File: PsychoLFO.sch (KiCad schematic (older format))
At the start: 17 parts

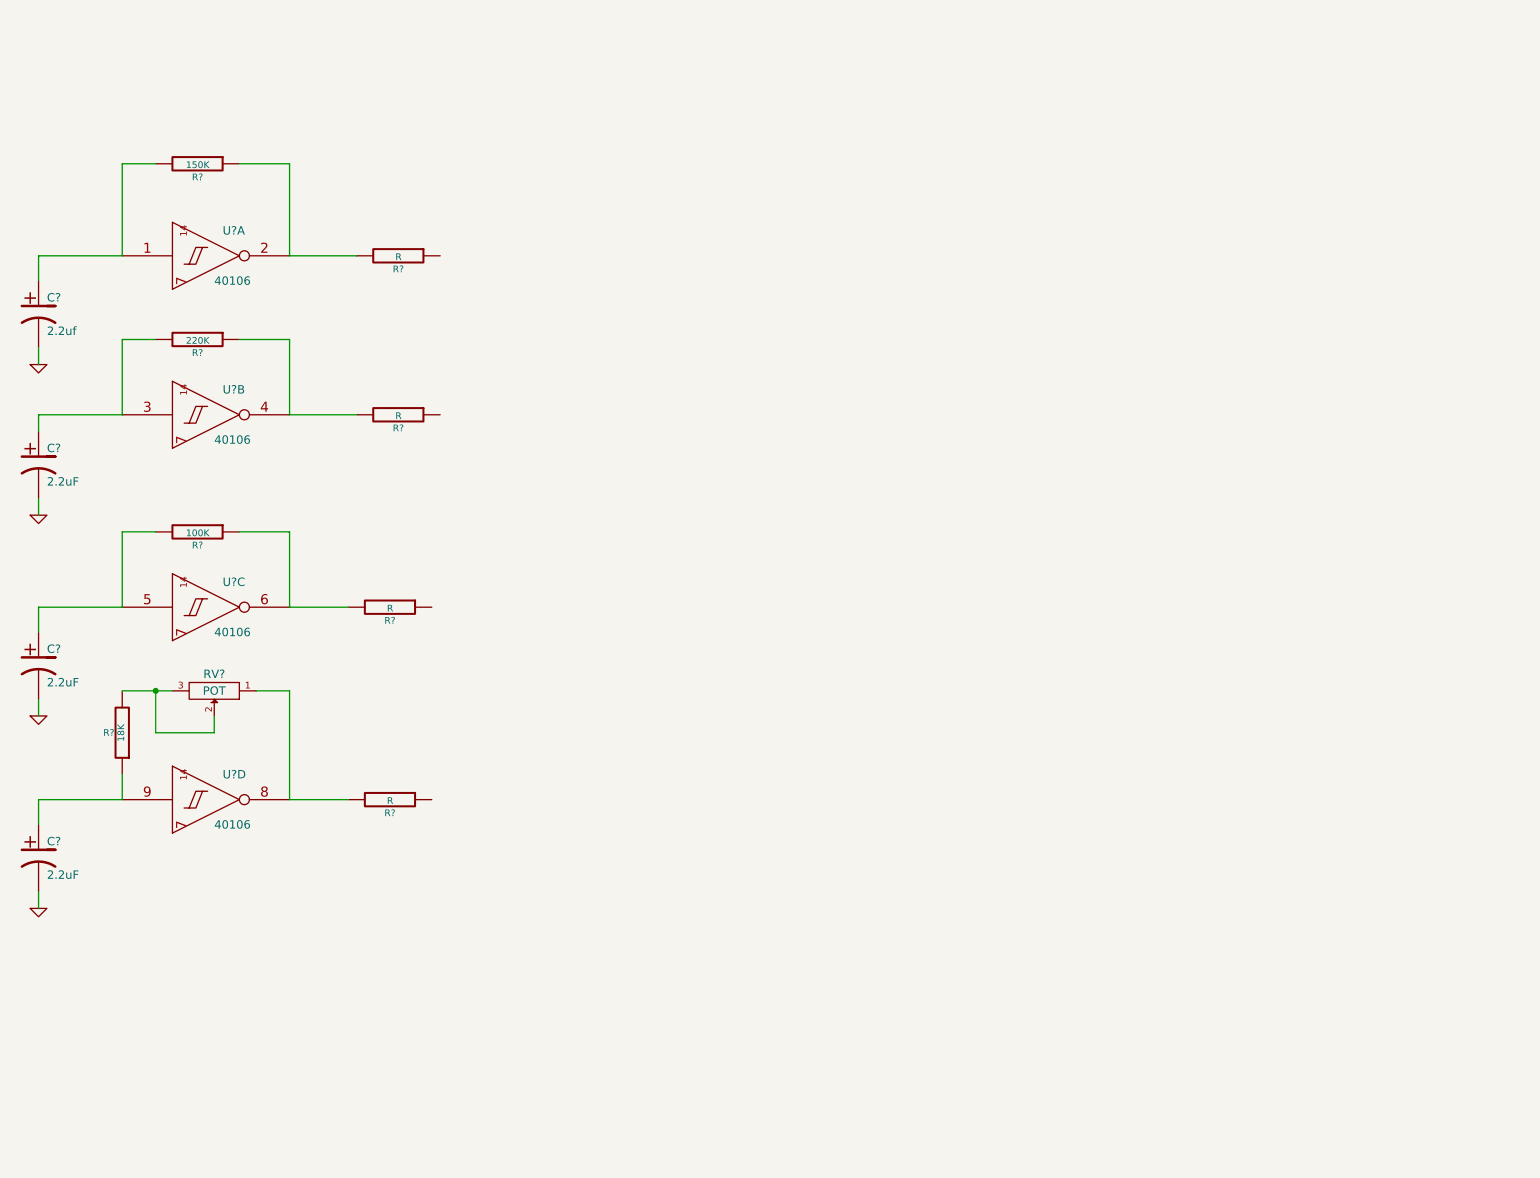
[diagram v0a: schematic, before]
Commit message: Some further progress on LFO
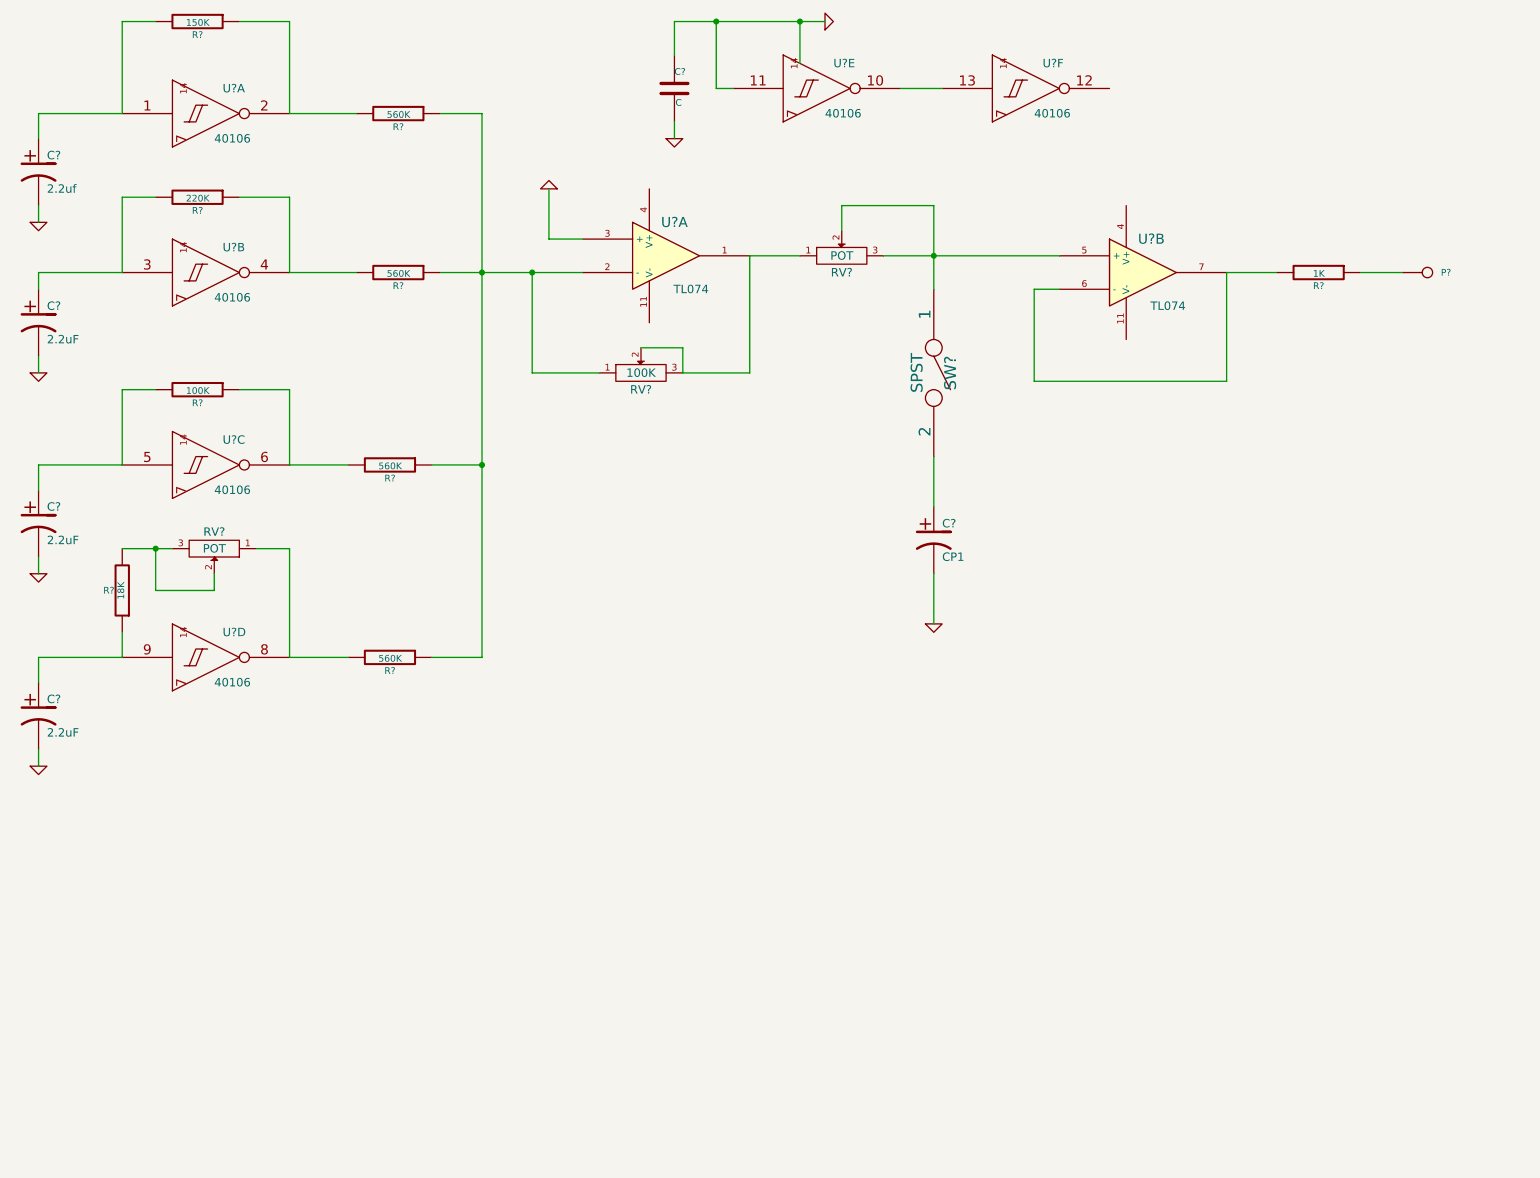
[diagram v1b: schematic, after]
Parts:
- added C?: CP1, symbol CP1
- added C?: C, symbol C
- added P?: CONN_1, symbol CONN_1
- added R?: 1K, symbol R
- added RV?: 100K, symbol POT
- added RV?: POT, symbol POT
- added SW?: SPST, symbol SPST
- added U? (x2): TL074, symbol TL074
- added U? (x2): 40106, symbol 40106
- R? (x4): value R -> 560K
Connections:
- net GND: now also C?.1, C?.2, C?.2, U?.11 (In), U?.14 (VDD), U?.3 (+)
- net at R?.1: now also R?.1, R?.1, R?.1, RV?.1, U?.2 (-)
- new net: RV?.1, RV?.2, RV?.3, U?.1
- new net: RV?.2, RV?.3, SW?.1, U?.5 (+)
- new net: C?.1, SW?.2
- new net: R?.2, U?.6 (-), U?.7
- new net: P?.1, R?.1
- new net: U?.10 (Out), U?.13 (In)
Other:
- moved on the sheet: C?, R?, RV?, U?A, U?B, U?C, U?D

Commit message: Added CV Mixer section
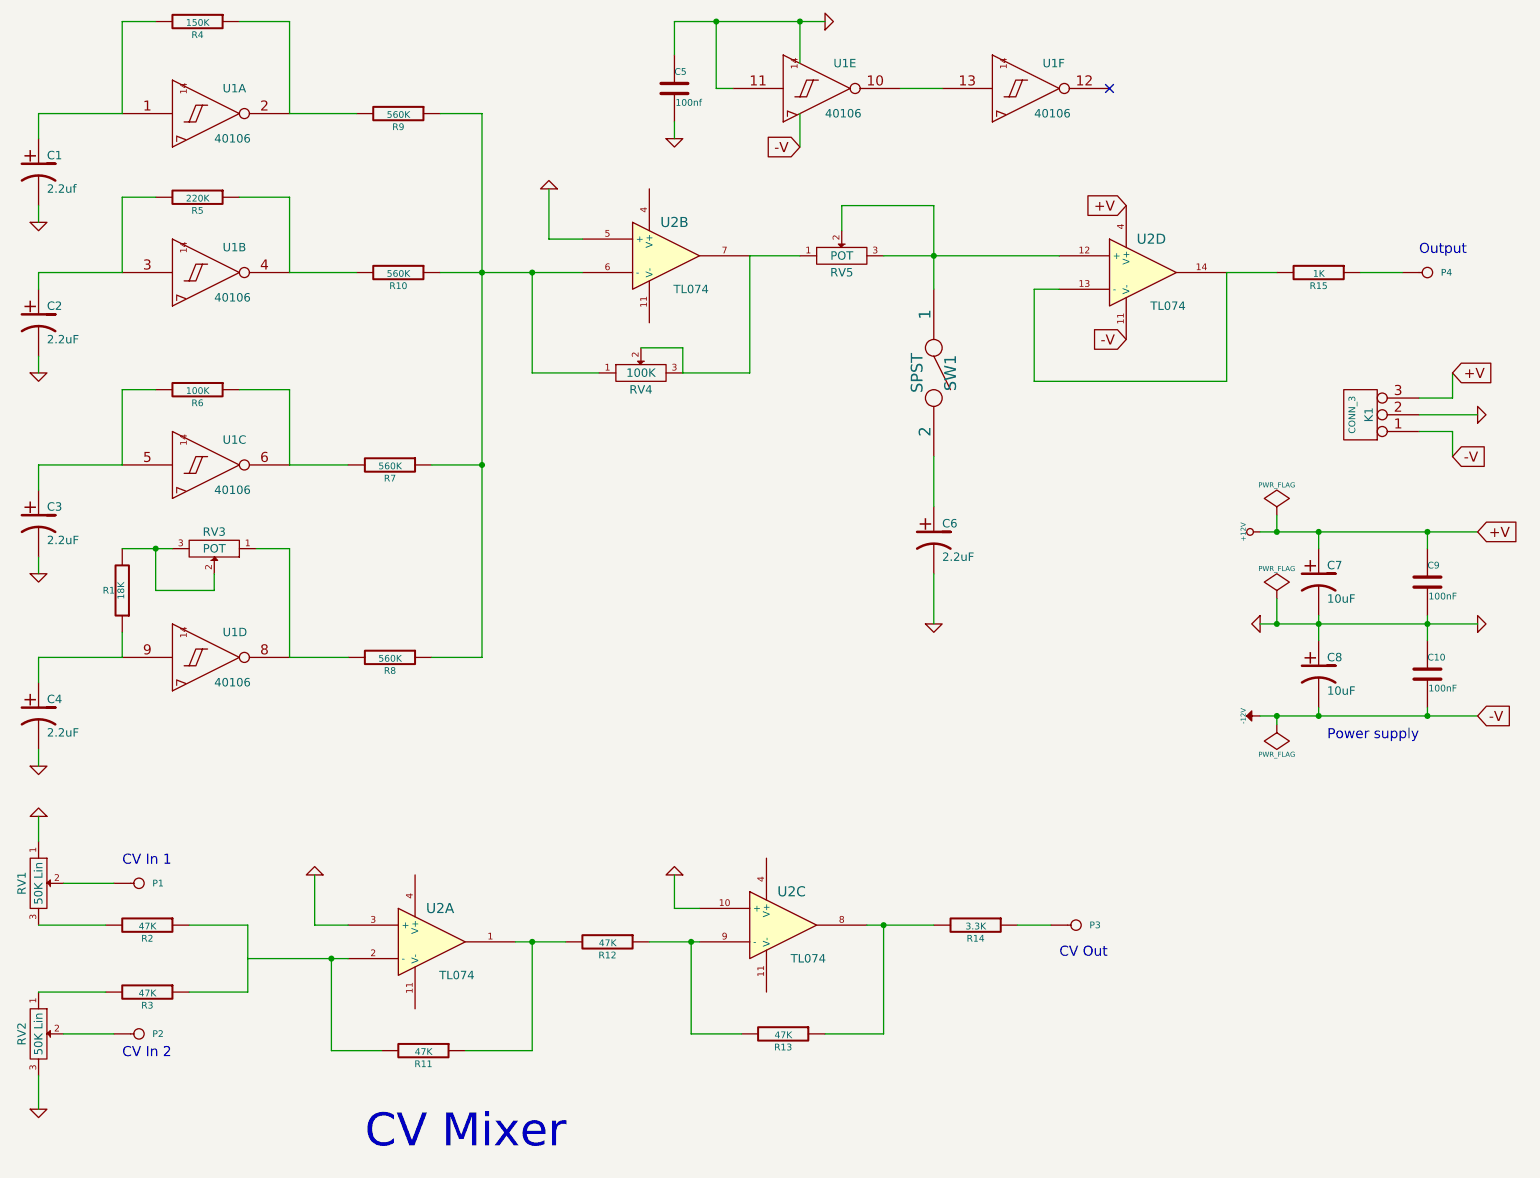
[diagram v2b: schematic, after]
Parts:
- added C10, C9: 100nF, symbol C
- added C7, C8: 10uF, symbol CP1
- added K1: CONN_3, symbol CONN_3
- added P1, P2, P3: CONN_1, symbol CONN_1
- added R11, R12, R13, R2, R3: 47K, symbol R
- added R14: 3.3K, symbol R
- added RV1, RV2: 50K Lin, symbol POT
- added unit 1 of U2
- added unit 3 of U2
- C5: renamed from C?; value C -> 100nf
- C6: renamed from C?; value CP1 -> 2.2uF
- P4: renamed from P?; value CONN_1 -> Out
- gave numbers to parts that had none: 19
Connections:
- net GND: now also U2.5 (+), C10.1, C7.2, C8.1, C9.2, K1.2 (PM), RV1.1, RV2.3, U2.10 (+), U2.3 (+); no longer U2.3 (+)
- net at R10.1, R7.1, R8.1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: now also U2.6 (-); no longer U2.2 (-)
- net at RV4.2, RV4.3, RV5.1: now also U2.7; no longer U2.1
- net at RV5.2, RV5.3, SW1.1: now also U2.12 (+); no longer U2.5 (+)
- net -12V: now reaches U2.11 (V-)
- net -12V: now also U1.7 (VSS), C10.2, C8.2, K1.1 (P1)
- net +12V: now reaches U2.4 (V+)
- net +12V: now also C7.1, C9.1, K1.3 (P3)
- new net: R15.2, U2.13 (-), U2.14
- new net: R11.1, R12.2, U2.1
- new net: R11.2, U2.2 (-)
- new net: R13.1, R14.2, U2.8
- new net: R12.1, R13.2, U2.9 (-)
- new net: R2.1, R3.1
- new net: R2.2, RV1.3
- new net: R3.2, RV2.1
- new net: P1.1, RV1.2
- new net: P2.1, RV2.2
- new net: P3.1, R14.1
- no-connect marks 0 -> 1
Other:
- note added: "CV In 1"
- note added: "CV In 2"
- note added: "CV Mixer"
- note added: "CV Out"
- note added: "Output"
- note added: "Power supply"
